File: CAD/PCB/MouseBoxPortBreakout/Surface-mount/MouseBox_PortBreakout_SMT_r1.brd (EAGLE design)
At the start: 24.4 x 49.8 mm, 7 parts

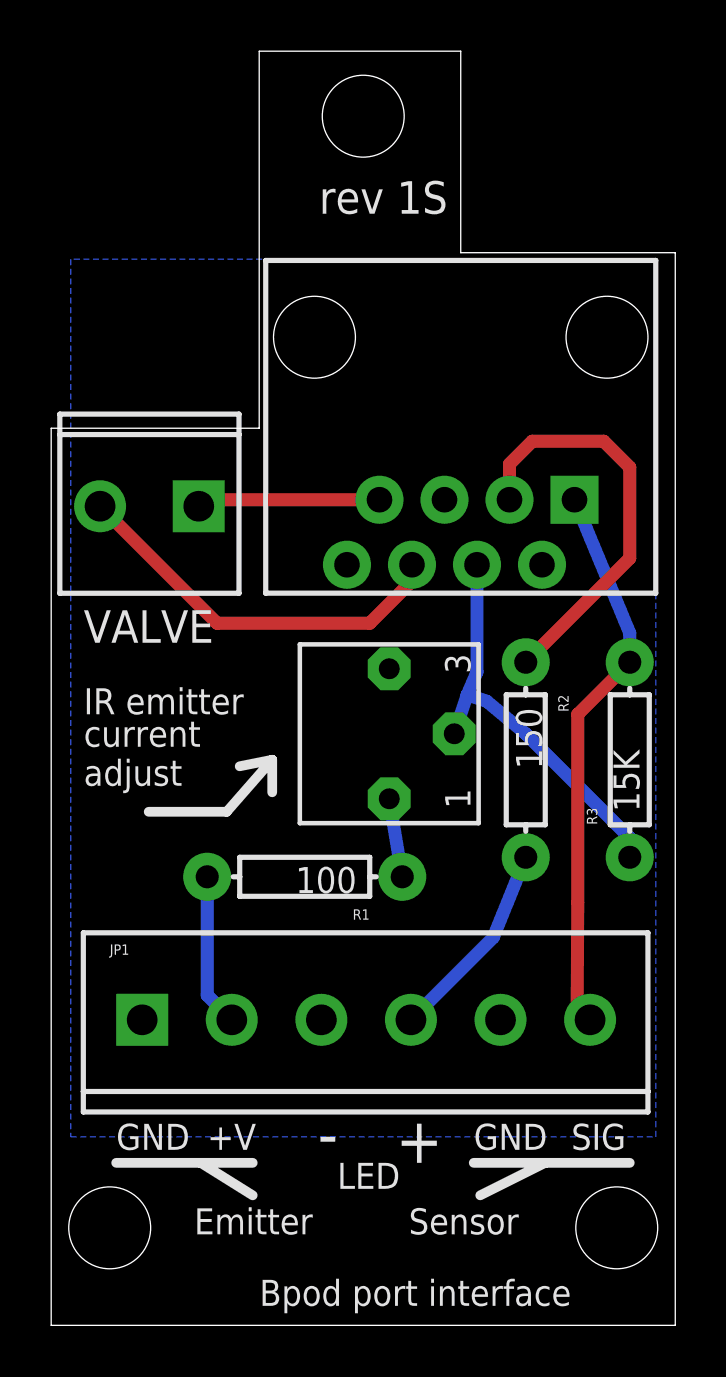
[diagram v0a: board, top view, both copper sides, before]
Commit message: -Updated design for mouse box port breakout board -Added a surface mount version of the port breakout board
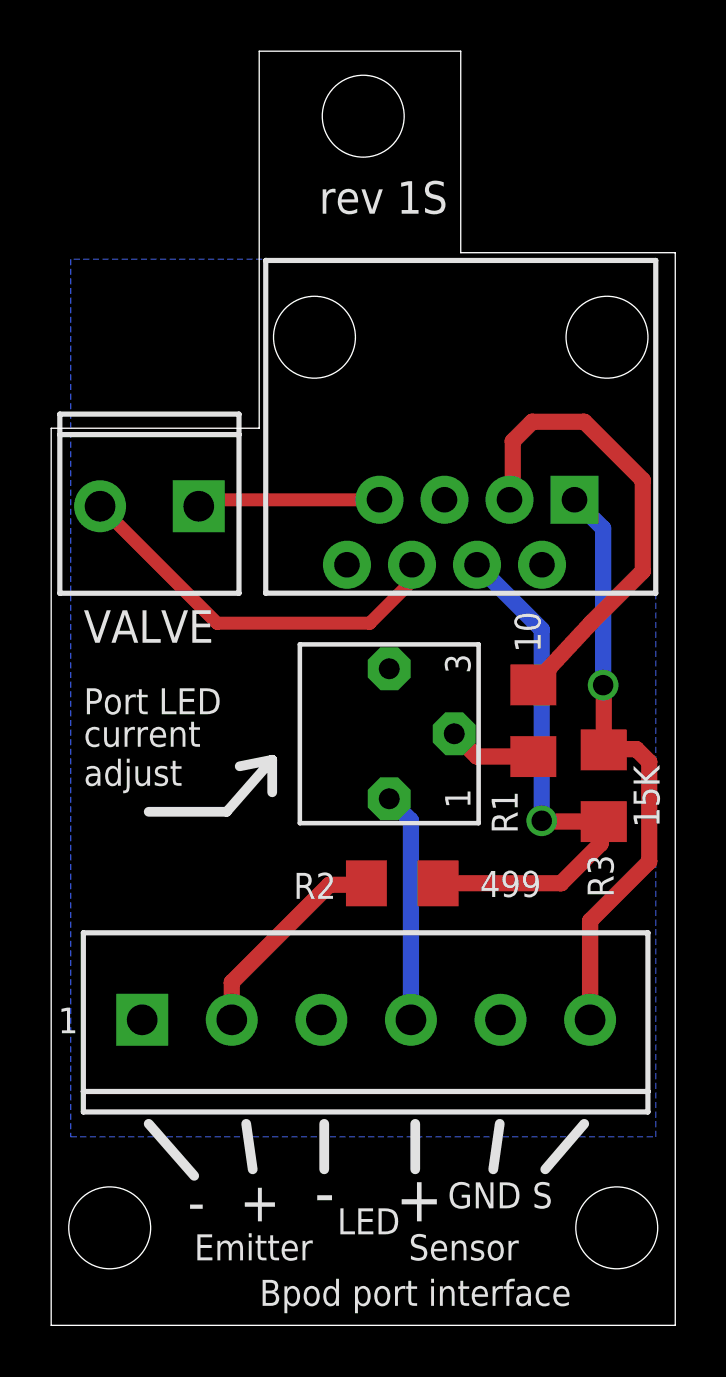
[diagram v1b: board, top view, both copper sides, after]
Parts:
- R1: value 100 -> 10; device SparkFun-Resistors:AXIAL-0.3 -> SparkFun-Resistors:1206
- R2: value 150 -> 499; device SparkFun-Resistors:AXIAL-0.3 -> SparkFun-Resistors:1206
- R3: device SparkFun-Resistors:AXIAL-0.3 -> SparkFun-Resistors:1206
- moved R1 10.8 mm to (36.9, 38.6), turned to 90 degrees
- moved R2 6.82 mm to (31.8, 32.3), turned to 180 degrees
- moved R3 1.44 mm to (39.6, 36.1)
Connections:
- removed net N$9: R1.P$1, R4.1
- new net N$4: R1.1, R4.2
- net N$1: now also R3.2; no longer R3.P$2
- net N$2: now also R2.1, R3.1; no longer R3.P$1, R4.2
- net N$3: now also R2.2; no longer R1.P$2
- net N$7: now also R4.1; no longer R2.P$2
- net N$8: now also R1.2; no longer R2.P$1
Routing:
- net N$2: track 16.1 -> 21.4 mm, vias 0 -> 1
- net N$4: track 0.00 -> 3.46 mm
- net N$9: track 3.09 -> 0.00 mm
- net N$3: track 5.99 -> 8.33 mm
- net N$8: track 16.2 -> 18.4 mm
- net N$7: track 7.93 -> 8.99 mm
- net N$1: track 22.4 -> 23.3 mm, vias 0 -> 1
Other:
- board text added: "1"
- board text added: "Port LED"
- board text added: "S"
- board text removed: "+V"
- board text removed: "IR emitter"
- board text removed: "SIG"
